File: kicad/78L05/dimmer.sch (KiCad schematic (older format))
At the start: 9 parts, among them IC1 ATTINY85-S, P1 CONN_01X02, P2 CONN_01X02, Q1 Q_NMOS_GDS, SW2 TACTILE_SW, SW4 TACTILE_SW, U1 MC78L05ACH

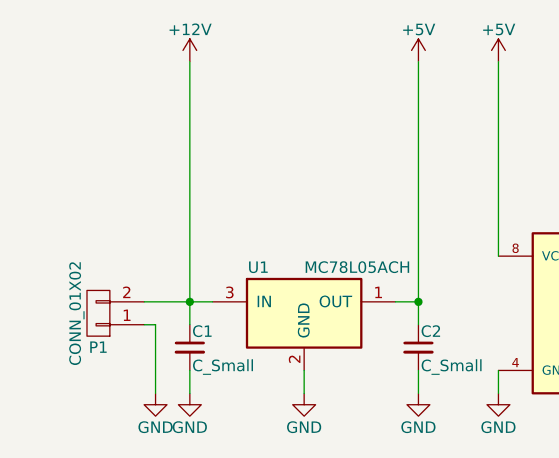
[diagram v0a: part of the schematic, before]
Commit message: 78L05 PCB: added guard diode
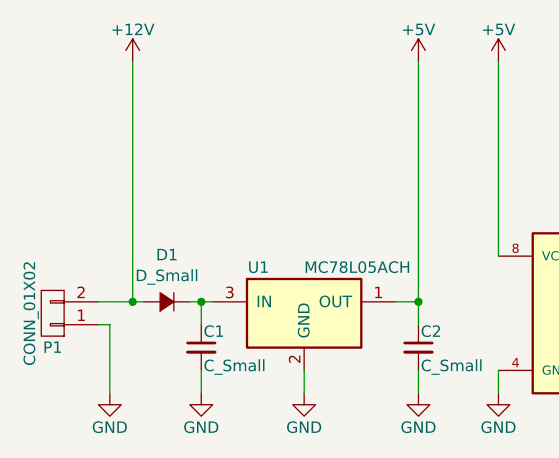
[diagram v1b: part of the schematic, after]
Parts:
- added D1: D_Small, Diodes_SMD:SMA_Standard, symbol D_Small
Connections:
- net +12V: now also D1.2 (A); no longer C1.1, U1.3 (IN)
- new net: C1.1, D1.1 (K), U1.3 (IN)
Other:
- moved on the sheet: C1, P1
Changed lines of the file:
@@
 EESchema Schematic File Version 2
-LIBS:power
-LIBS:device
-LIBS:transistors
-LIBS:conn
-LIBS:linear
-LIBS:regul
-LIBS:74xx
-LIBS:cmos4000
-LIBS:adc-dac
-LIBS:memory
-LIBS:xilinx
-LIBS:microcontrollers
-LIBS:dsp
-LIBS:microchip
-LIBS:analog_switches
-LIBS:motorola
-LIBS:texas
-LIBS:intel
-LIBS:audio
-LIBS:interface
-LIBS:digital-audio
-LIBS:philips
-LIBS:display
-LIBS:cypress
-LIBS:siliconi
-LIBS:opto
-LIBS:atmel
-LIBS:contrib
-LIBS:valves
-LIBS:irlz44nto220v
-LIBS:button
 LIBS:dimmer-cache
 EELAYER 25 0
@@
 L +12V #PWR02
 U 1 1 57A73161
-P 2550 2000
-F 0 "#PWR02" H 2550 1850 50  0001 C CNN
-F 1 "+12V" H 2550 2140 50  0000 C CNN
-F 2 "" H 2550 2000 50  0000 C CNN
-F 3 "" H 2550 2000 50  0000 C CNN
-	1    2550 2000
+P 2300 2000
+F 0 "#PWR02" H 2300 1850 50  0001 C CNN
+F 1 "+12V" H 2300 2140 50  0000 C CNN
+F 2 "" H 2300 2000 50  0000 C CNN
+F 3 "" H 2300 2000 50  0000 C CNN
+	1    2300 2000
 	1    0    0    -1
 $EndComp
@@
 L CONN_01X02 P1
 U 1 1 57A7320A
-P 2150 3100
-F 0 "P1" H 2150 3250 50  0000 C CNN
-F 1 "CONN_01X02" V 2250 3100 50  0000 C CNN
-F 2 "con-wago-508:W237-132" H 2150 3100 50  0001 C CNN
-F 3 "" H 2150 3100 50  0000 C CNN
-	1    2150 3100
+P 1950 3100
+F 0 "P1" H 1950 3250 50  0000 C CNN
+F 1 "CONN_01X02" V 2050 3100 50  0000 C CNN
+F 2 "con-wago-508:W237-132" H 1950 3100 50  0001 C CNN
+F 3 "" H 1950 3100 50  0000 C CNN
+	1    1950 3100
 	-1   0    0    1
 $EndComp
@@
 L C_Small C1
 U 1 1 57A73350
-P 2550 3250
-F 0 "C1" H 2560 3320 50  0000 L CNN
-F 1 "C_Small" H 2560 3170 50  0000 L CNN
-F 2 "Capacitors_SMD:C_0805" H 2550 3250 50  0001 C CNN
-F 3 "" H 2550 3250 50  0000 C CNN
-	1    2550 3250
+P 2600 3250
+F 0 "C1" H 2610 3320 50  0000 L CNN
+F 1 "C_Small" H 2610 3170 50  0000 L CNN
+F 2 "Capacitors_SMD:C_0805" H 2600 3250 50  0001 C CNN
+F 3 "" H 2600 3250 50  0000 C CNN
+	1    2600 3250
 	1    0    0    -1
 $EndComp
@@
 	3900 2850 3900 2000
 Wire Wire Line
-	2350 3050 2650 3050
-Wire Wire Line
-	2550 2000 2550 3150
-Connection ~ 2550 3050
-Wire Wire Line
-	2350 3150 2400 3150
-Wire Wire Line
-	2400 3150 2400 3450
+	2150 3150 2200 3150
+Wire Wire Line
+	2200 3150 2200 3450
 Wire Wire Line
 	3050 3350 3050 3450
@@
 	3550 3450 3550 3350
 Wire Wire Line
-	2550 3450 2550 3350
+	2600 3450 2600 3350
 Wire Wire Line
 	6600 3250 7700 3250
@@
 	8050 2950 8050 2750
 $Comp
-L +12V #PWR05
+L +12V #PWR04
 U 1 1 57A7493A
 P 8050 2000
-F 0 "#PWR05" H 8050 1850 50  0001 C CNN
+F 0 "#PWR04" H 8050 1850 50  0001 C CNN
 F 1 "+12V" H 8050 2140 50  0000 C CNN
 F 2 "" H 8050 2000 50  0000 C CNN
@@
 out
 $Comp
+L GND #PWR05
+U 1 1 57A75236
+P 2200 3450
+F 0 "#PWR05" H 2200 3200 50  0001 C CNN
+F 1 "GND" H 2200 3300 50  0000 C CNN
+F 2 "" H 2200 3450 50  0000 C CNN
+F 3 "" H 2200 3450 50  0000 C CNN
+	1    2200 3450
+	1    0    0    -1
+$EndComp
+$Comp
 L GND #PWR06
-U 1 1 57A75236
-P 2400 3450
-F 0 "#PWR06" H 2400 3200 50  0001 C CNN
-F 1 "GND" H 2400 3300 50  0000 C CNN
-F 2 "" H 2400 3450 50  0000 C CNN
-F 3 "" H 2400 3450 50  0000 C CNN
-	1    2400 3450
+U 1 1 57A7526C
+P 2600 3450
+F 0 "#PWR06" H 2600 3200 50  0001 C CNN
+F 1 "GND" H 2600 3300 50  0000 C CNN
+F 2 "" H 2600 3450 50  0000 C CNN
+F 3 "" H 2600 3450 50  0000 C CNN
+	1    2600 3450
 	1    0    0    -1
 $EndComp
 $Comp
 L GND #PWR07
-U 1 1 57A7526C
-P 2550 3450
-F 0 "#PWR07" H 2550 3200 50  0001 C CNN
-F 1 "GND" H 2550 3300 50  0000 C CNN
-F 2 "" H 2550 3450 50  0000 C CNN
-F 3 "" H 2550 3450 50  0000 C CNN
-	1    2550 3450
-	1    0    0    -1
-$EndComp
-$Comp
-L GND #PWR08
 U 1 1 57A7529B
 P 3050 3450
-F 0 "#PWR08" H 3050 3200 50  0001 C CNN
+F 0 "#PWR07" H 3050 3200 50  0001 C CNN
 F 1 "GND" H 3050 3300 50  0000 C CNN
 F 2 "" H 3050 3450 50  0000 C CNN
@@
 $EndComp
 $Comp
-L GND #PWR09
+L GND #PWR08
 U 1 1 57A752E2
 P 3550 3450
-F 0 "#PWR09" H 3550 3200 50  0001 C CNN
+F 0 "#PWR08" H 3550 3200 50  0001 C CNN
 F 1 "GND" H 3550 3300 50  0000 C CNN
 F 2 "" H 3550 3450 50  0000 C CNN
@@
 $EndComp
 $Comp
-L GND #PWR010
+L GND #PWR09
 U 1 1 57A75311
 P 3900 3450
-F 0 "#PWR010" H 3900 3200 50  0001 C CNN
+F 0 "#PWR09" H 3900 3200 50  0001 C CNN
 F 1 "GND" H 3900 3300 50  0000 C CNN
 F 2 "" H 3900 3450 50  0000 C CNN
@@
 $EndComp
 $Comp
-L GND #PWR011
+L GND #PWR010
 U 1 1 57A753DC
 P 7600 3450
-F 0 "#PWR011" H 7600 3200 50  0001 C CNN
+F 0 "#PWR010" H 7600 3200 50  0001 C CNN
 F 1 "GND" H 7600 3300 50  0000 C CNN
 F 2 "" H 7600 3450 50  0000 C CNN
@@
 $EndComp
 $Comp
-L GND #PWR012
+L GND #PWR011
 U 1 1 57A7540B
 P 8050 3450
-F 0 "#PWR012" H 8050 3200 50  0001 C CNN
+F 0 "#PWR011" H 8050 3200 50  0001 C CNN
 F 1 "GND" H 8050 3300 50  0000 C CNN
 F 2 "" H 8050 3450 50  0000 C CNN
@@
 $Comp
 L ATTINY85-S IC1
-U 1 1 57AF71E0
+U 1 1 58053039
 P 5250 3100
 F 0 "IC1" H 5250 3707 50  0000 C CNN
@@
 	-1   0    0    -1
 $EndComp
+Wire Wire Line
+	2150 3050 2350 3050
+$Comp
+L D_Small D1
+U 1 1 5805316F
+P 2450 3050
+F 0 "D1" H 2450 3255 50  0000 C CNN
+F 1 "D_Small" H 2450 3164 50  0000 C CNN
+F 2 "Diodes_SMD:SMA_Standard" V 2450 3050 50  0001 C CNN
+F 3 "" V 2450 3050 50  0000 C CNN
+	1    2450 3050
+	-1   0    0    -1
+$EndComp
+Wire Wire Line
+	2550 3050 2650 3050
+Wire Wire Line
+	2300 2000 2300 3050
+Connection ~ 2300 3050
+Wire Wire Line
+	2600 3150 2600 3050
+Connection ~ 2600 3050
 $EndSCHEMATC
